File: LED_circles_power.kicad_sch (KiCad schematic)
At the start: 12 parts, among them J2 USB_C_Receptacle_PowerOnly_6P, U74 BD33GA3WEFJ

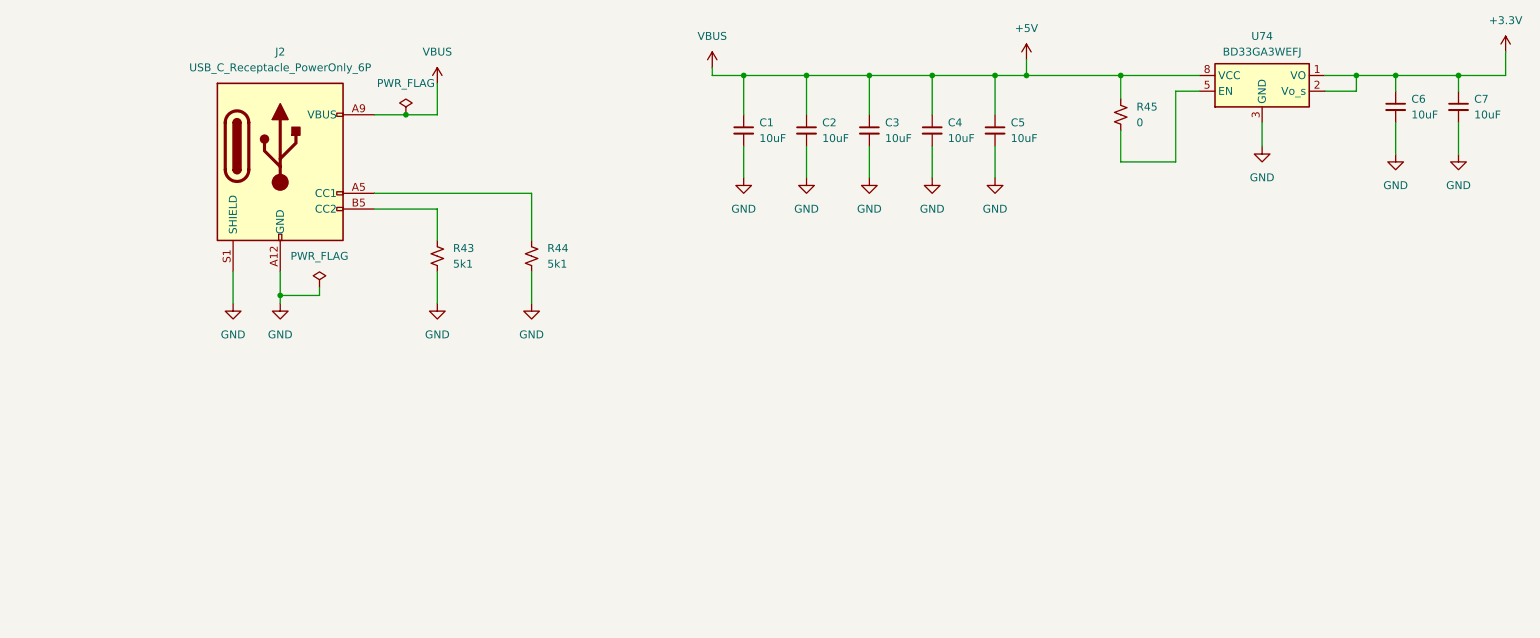
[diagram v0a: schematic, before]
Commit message: Changed micro controller to larger package
- Also changed PCB DRC to work with OSH Park
- Changed SWD connection to generic  0.1" pogopin headers
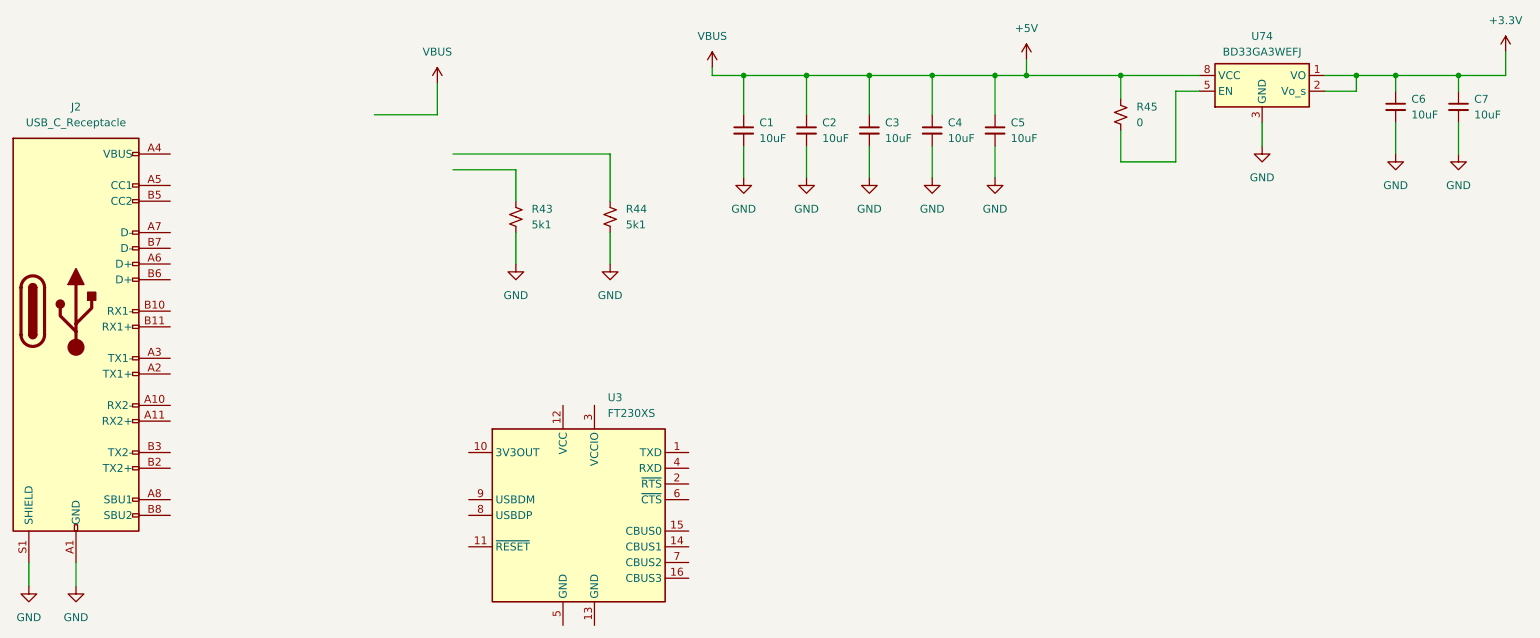
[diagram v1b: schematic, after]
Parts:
- added U3: FT230XS, Package_SO:SSOP-16_3.9x4.9mm_P0.635mm, symbol Interface_USB:FT230XS
- J2: value USB_C_Receptacle_PowerOnly_6P -> USB_C_Receptacle; symbol Connector:USB_C_Receptacle_PowerOnly_6P -> Connector:USB_C_Receptacle
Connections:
- net +5V: no longer J2.A9 (VBUS), J2.B9 (VBUS)
- net GND: now also J2.A1 (GND), J2.B1 (GND)
- net at R44.1: no longer J2.A5 (CC1)
- net at R43.1: no longer J2.B5 (CC2)
- new net: J2.A4 (VBUS), J2.A9 (VBUS), J2.B4 (VBUS), J2.B9 (VBUS)
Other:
- moved on the sheet: R43, R44

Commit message: reverted back to power only USB
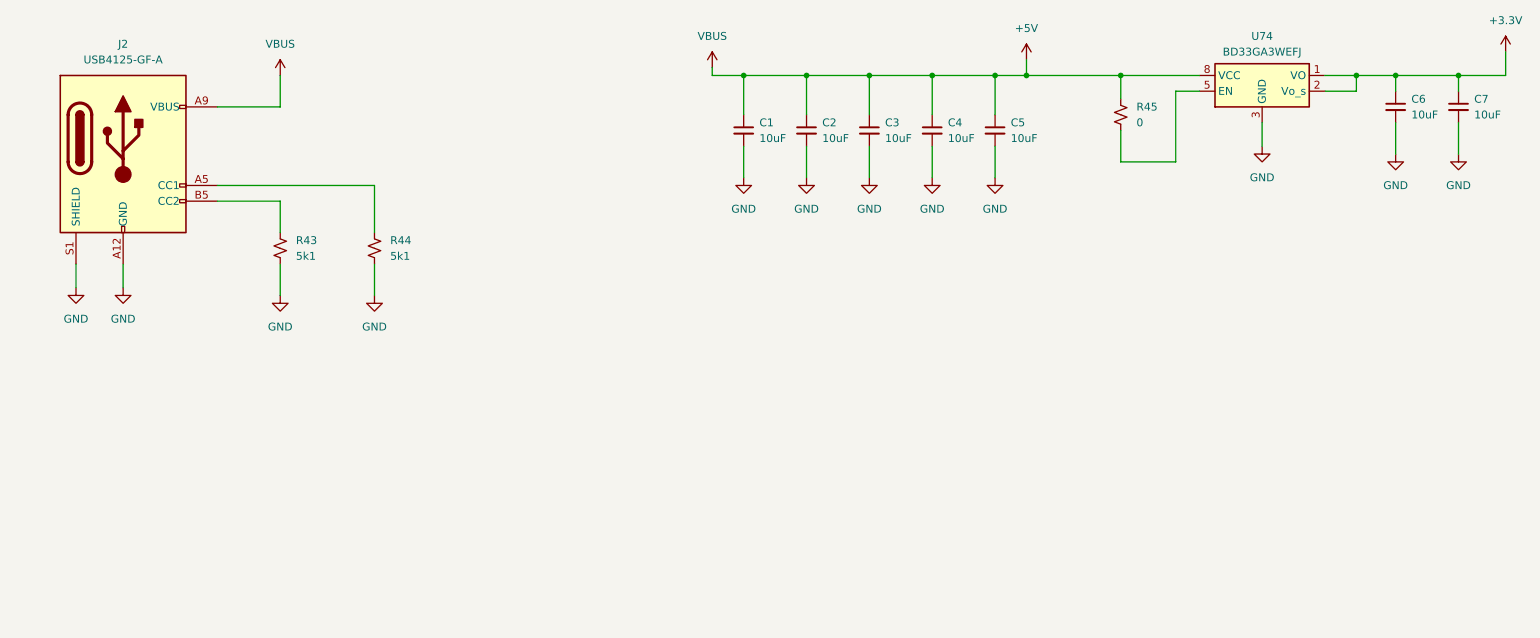
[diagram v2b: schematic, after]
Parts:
- removed J2: USB_C_Receptacle, Connector_USB:USB_C_Receptacle_GCT_USB4125-xx-x-0190_6P_TopMnt_Horizontal, symbol Connector:USB_C_Receptacle
- removed U3: FT230XS, Package_SO:SSOP-16_3.9x4.9mm_P0.635mm, symbol Interface_USB:FT230XS
- added J2: USB4125-GF-A, Connector_USB:USB_C_Receptacle_GCT_USB4125-xx-x-0190_6P_TopMnt_Horizontal, symbol Connector:USB_C_Receptacle_PowerOnly_6P
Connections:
- net +5V: now also J2.A9 (VBUS), J2.B9 (VBUS)
- net GND: now also J2.A12 (GND), J2.B12 (GND), J2.S1 (SHIELD)
- net at R44.1: now also J2.A5 (CC1)
- net at R43.1: now also J2.B5 (CC2)
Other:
- moved on the sheet: R43, R44
